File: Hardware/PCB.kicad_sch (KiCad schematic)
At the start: 13 parts, among them J2 Conn_01x06, SW1 SW_MEC_5E, U1 ME54BS01_V1.0, U3 MCP1700x-330xxTT

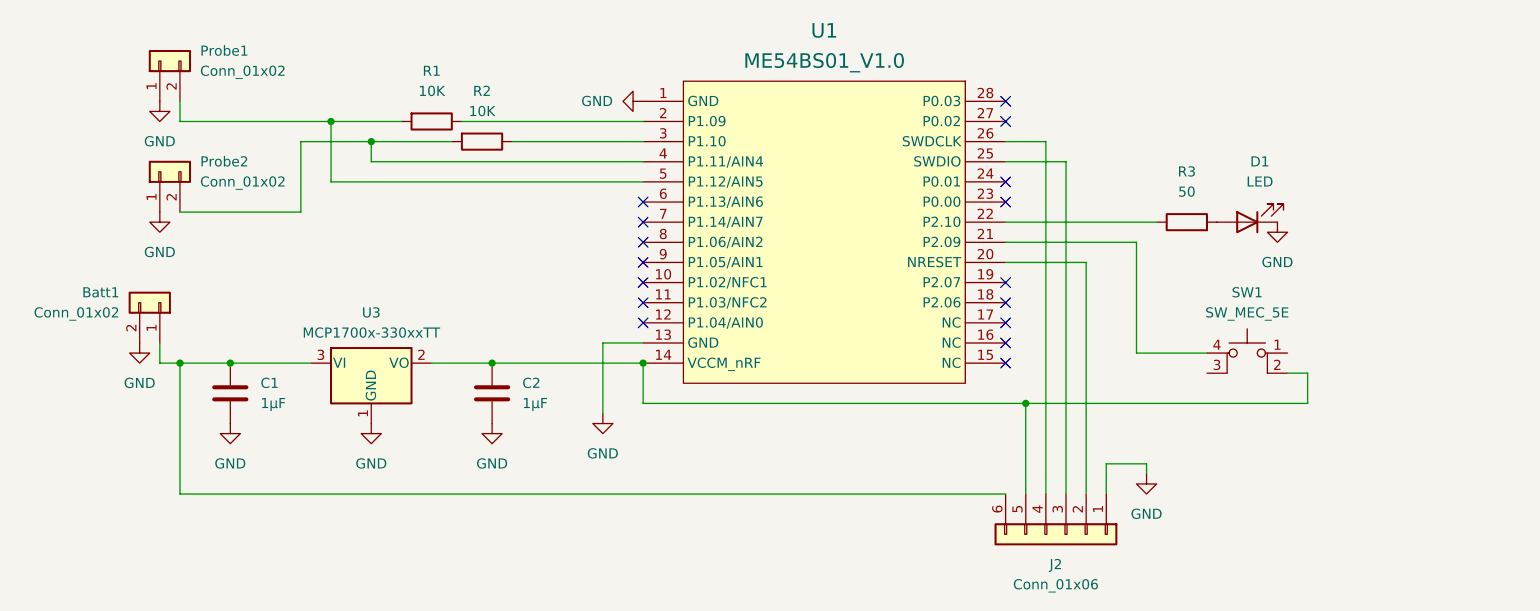
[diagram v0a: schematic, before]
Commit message: Revision 2 of the PCB using all SMD components
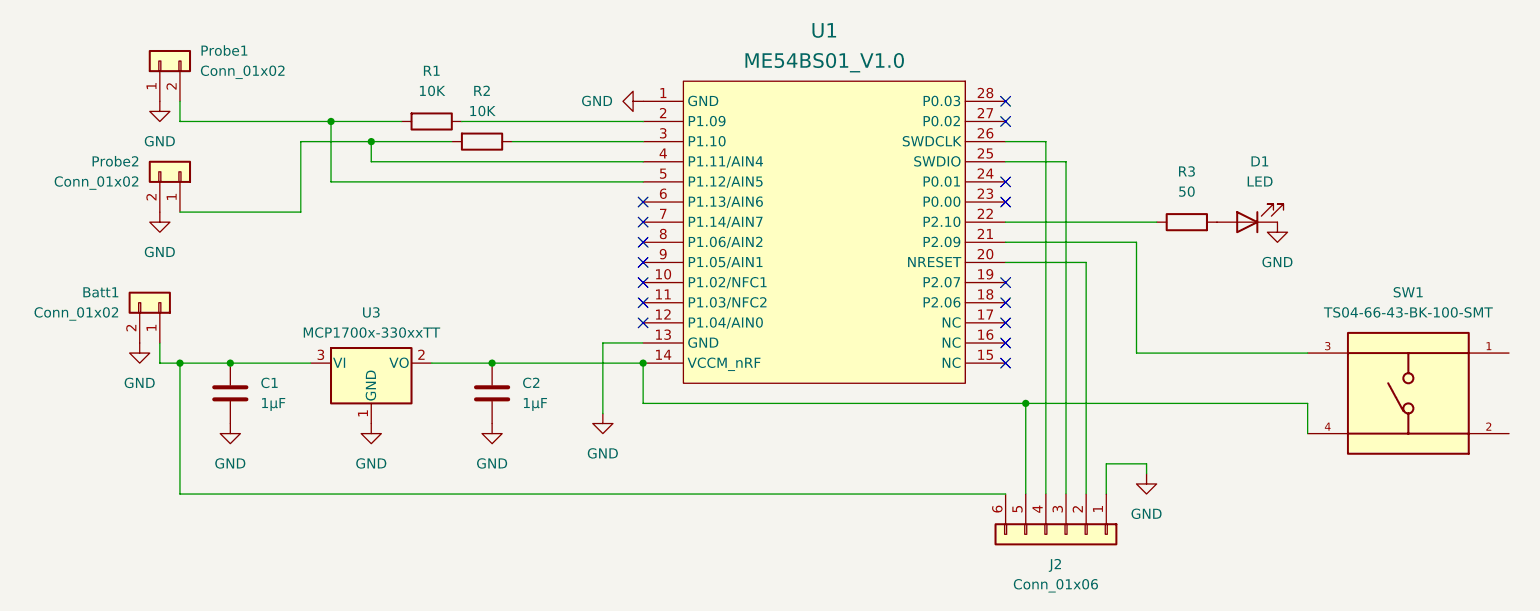
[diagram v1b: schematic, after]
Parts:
- removed SW1: SW_MEC_5E, TS02-66-55-BK-100-LCR-D:SW_TS02-66-55-BK-100-LCR-D, symbol Switch:SW_MEC_5E
- added SW1: TS04-66-43-BK-100-SMT, TS04-66-43-BK-100-SMT:SW_TS04-66-43-BK-100-SMT, symbol TS04-66-43-BK-100-SMT:TS04-66-43-BK-100-SMT
- Batt1, Probe1, Probe2: footprint Connector_JST:JST_PH_S2B-PH-K_1x02_P2.00mm_Horizontal -> S2B-PH-SM4-TB:JST_S2B-PH-SM4-TB
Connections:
- net GND: now also Probe2.2 (Pin_2); no longer Probe2.1 (Pin_1)
- net at C2.1, J2.5 (Pin_5), U1.14 (VCCM_nRF)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: now also SW1.4
- net at U1.21 (P2.09): now also SW1.3
- net at R2.2, U1.4 (P1.11/AIN4): now also Probe2.1 (Pin_1); no longer Probe2.2 (Pin_2)
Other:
- moved on the sheet: Probe2
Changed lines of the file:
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@@
 	(wire
 		(pts
-			(xy 217.17 59.69) (xy 226.06 59.69)
+			(xy 217.17 59.69) (xy 238.76 59.69)
 		)
 		(stroke
@@
 	(wire
 		(pts
-			(xy 238.76 62.23) (xy 238.76 66.04)
-		)
-		(stroke
-			(width 0)
-			(type default)
-		)
-	)
-	(wire
-		(pts
 			(xy 205.74 33.02) (xy 200.66 33.02)
 		)
@@
 	(wire
 		(pts
-			(xy 236.22 62.23) (xy 238.76 62.23)
-		)
-		(stroke
-			(width 0)
-			(type default)
-		)
-	)
-	(wire
-		(pts
 			(xy 200.66 35.56) (xy 208.28 35.56)
+		)
+		(stroke
+			(width 0)
+			(type default)
+		)
+	)
+	(wire
+		(pts
+			(xy 238.76 66.04) (xy 238.76 69.85)
 		)
 		(stroke
@@
 	)
 	(symbol
-		(lib_id "Switch:SW_MEC_5E")
-		(at 231.14 62.23 0)
-		(mirror y)
-		(unit 1)
-		(exclude_from_sim no)
-		(in_bom yes)
-		(on_board yes)
-		(dnp no)
-		(property "Reference" "SW1"
-			(at 231.14 52.07 0)
-			(effects
-				(font
-					(size 1.27 1.27)
-				)
-			)
-		)
-		(property "Value" "SW_MEC_5E"
-			(at 231.14 54.61 0)
-			(effects
-				(font
-					(size 1.27 1.27)
-				)
-			)
-		)
-		(property "Footprint" "TS02-66-55-BK-100-LCR-D:SW_TS02-66-55-BK-100-LCR-D"
-			(at 231.14 54.61 0)
-			(effects
-				(font
-					(size 1.27 1.27)
-				)
-				(hide yes)
-			)
-		)
-		(property "Datasheet" "http://www.apem.com/int/index.php?controller=attachment&id_attachment=1371"
-			(at 231.14 54.61 0)
-			(effects
-				(font
-					(size 1.27 1.27)
-				)
-				(hide yes)
-			)
-		)
-		(property "Description" "MEC 5E single pole normally-open tactile switch"
-			(at 231.14 62.23 0)
-			(effects
-				(font
-					(size 1.27 1.27)
-				)
-				(hide yes)
-			)
-		)
-		(pin "1"
-		)
-		(pin "4"
-		)
-		(pin "2"
-		)
-		(pin "3"
-		)
-		(instances
-			(project ""
-				(path "/9240e15d-484a-49b3-8f80-37d1a010783e"
-					(reference "SW1")
-					(unit 1)
-				)
-			)
-		)
-	)
-	(symbol
 		(lib_id "Connector_Generic:Conn_01x02")
 		(at 93.98 22.86 90)
@@
 			)
 		)
-		(property "Footprint" "Connector_JST:JST_PH_S2B-PH-K_1x02_P2.00mm_Horizontal"
+		(property "Footprint" "S2B-PH-SM4-TB:JST_S2B-PH-SM4-TB"
 			(at 93.98 22.86 0)
 			(effects
@@
 	(symbol
 		(lib_id "Connector_Generic:Conn_01x02")
-		(at 93.98 36.83 90)
+		(at 96.52 36.83 270)
+		(mirror x)
 		(unit 1)
 		(exclude_from_sim no)
@@
 		(on_board yes)
 		(dnp no)
-		(fields_autoplaced yes)
 		(property "Reference" "Probe2"
-			(at 99.06 35.5599 90)
+			(at 91.44 35.5599 90)
 			(effects
 				(font
@@
 		)
 		(property "Value" "Conn_01x02"
-			(at 99.06 38.0999 90)
+			(at 91.44 38.0999 90)
 			(effects
 				(font
@@
 			)
 		)
-		(property "Footprint" "Connector_JST:JST_PH_S2B-PH-K_1x02_P2.00mm_Horizontal"
-			(at 93.98 36.83 0)
+		(property "Footprint" "S2B-PH-SM4-TB:JST_S2B-PH-SM4-TB"
+			(at 96.52 36.83 0)
 			(effects
 				(font
@@
 		)
 		(property "Datasheet" "~"
-			(at 93.98 36.83 0)
+			(at 96.52 36.83 0)
 			(effects
 				(font
@@
 		)
 		(property "Description" "Generic connector, single row, 01x02, script generated (kicad-library-utils/schlib/autogen/connector/)"
-			(at 93.98 36.83 0)
+			(at 96.52 36.83 0)
 			(effects
 				(font
@@
 			)
 		)
-		(property "Footprint" "Connector_JST:JST_PH_S2B-PH-K_1x02_P2.00mm_Horizontal"
+		(property "Footprint" "S2B-PH-SM4-TB:JST_S2B-PH-SM4-TB"
 			(at 93.98 53.34 0)
 			(effects
@@
 					(unit 1)
 				)
+			)
+		)
+	)
+	(symbol
+		(lib_id "TS04-66-43-BK-100-SMT:TS04-66-43-BK-100-SMT")
+		(at 251.46 64.77 0)
+		(mirror y)
+		(unit 1)
+		(exclude_from_sim no)
+		(in_bom yes)
+		(on_board yes)
+		(dnp no)
+		(property "Reference" "SW1"
+			(at 251.46 52.07 0)
+			(effects
+				(font
+					(size 1.27 1.27)
+				)
+			)
+		)
+		(property "Value" "TS04-66-43-BK-100-SMT"
+			(at 251.46 54.61 0)
+			(effects
+				(font
+					(size 1.27 1.27)
+				)
+			)
+		)
+		(property "Footprint" "TS04-66-43-BK-100-SMT:SW_TS04-66-43-BK-100-SMT"
+			(at 251.46 64.77 0)
+			(effects
+				(font
+					(size 1.27 1.27)
+				)
+				(justify bottom)
+				(hide yes)
+			)
+		)
+		(property "Datasheet" ""
+			(at 251.46 64.77 0)
+			(effects
+				(font
+					(size 1.27 1.27)
+				)
+				(hide yes)
+			)
+		)
+		(property "Description" ""
+			(at 251.46 64.77 0)
+			(effects
+				(font
+					(size 1.27 1.27)
+				)
+				(hide yes)
+			)
+		)
+		(property "DigiKey_Part_Number" "2223-TS04-66-43-BK-100-SMT-ND"
+			(at 251.46 64.77 0)
+			(effects
+				(font
+					(size 1.27 1.27)
+				)
+				(justify bottom)
+				(hide yes)
+			)
+		)
+		(property "SnapEDA_Link" "https://www.snapeda.com/parts/TS04-66-43-BK-100-SMT/Same+Sky/view-part/?ref=snap"
+			(at 251.46 64.77 0)
+			(effects
+				(font
+					(size 1.27 1.27)
+				)
+				(justify bottom)
+				(hide yes)
+			)
+		)
+		(property "Description_1" "6 x 6 mm, 4.3 mm Actuator Height, 100 gf, Black, Surface Mount, SPST, Tactile Switch"
+			(at 251.46 64.77 0)
+			(effects
+				(font
+					(size 1.27 1.27)
+				)
+				(justify bottom)
+				(hide yes)
+			)
+		)
+		(property "Package" "None"
+			(at 251.46 64.77 0)
+			(effects
+				(font
+					(size 1.27 1.27)
+				)
+				(justify bottom)
+				(hide yes)
+			)
+		)
+		(property "Check_prices" "https://www.snapeda.com/parts/TS04-66-43-BK-100-SMT/Same+Sky/view-part/?ref=eda"
+			(at 251.46 64.77 0)
+			(effects
+				(font
+					(size 1.27 1.27)
+				)
+				(justify bottom)
+				(hide yes)
+			)
+		)
+		(property "STANDARD" "Manufacturer Recommendations"
+			(at 251.46 64.77 0)
+			(effects
+				(font
+					(size 1.27 1.27)
+				)
+				(justify bottom)
+				(hide yes)
+			)
+		)
+		(property "PARTREV" "1.0"
+			(at 251.46 64.77 0)
+			(effects
+				(font
+					(size 1.27 1.27)
+				)
+				(justify bottom)
+				(hide yes)
+			)
+		)
+		(property "MF" "Same Sky"
+			(at 251.46 64.77 0)
+			(effects
+				(font
+					(size 1.27 1.27)
+				)
+				(justify bottom)
+				(hide yes)
+			)
+		)
+		(property "MP" "TS04-66-43-BK-100-SMT"
+			(at 251.46 64.77 0)
+			(effects
+				(font
+					(size 1.27 1.27)
+				)
+				(justify bottom)
+				(hide yes)
+			)
+		)
+		(property "MANUFACTURER" "CUI Devices"
+			(at 251.46 64.77 0)
+			(effects
+				(font
+					(size 1.27 1.27)
+				)
+				(justify bottom)
+				(hide yes)
+			)
+		)
+		(pin "2"
+		)
+		(pin "3"
+		)
+		(pin "4"
+		)
+		(pin "1"
+		)
+		(instances
+			(project ""
+				(path "/9240e15d-484a-49b3-8f80-37d1a010783e"
+					(reference "SW1")
+					(unit 1)
+				)
